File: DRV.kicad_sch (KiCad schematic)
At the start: 31 parts

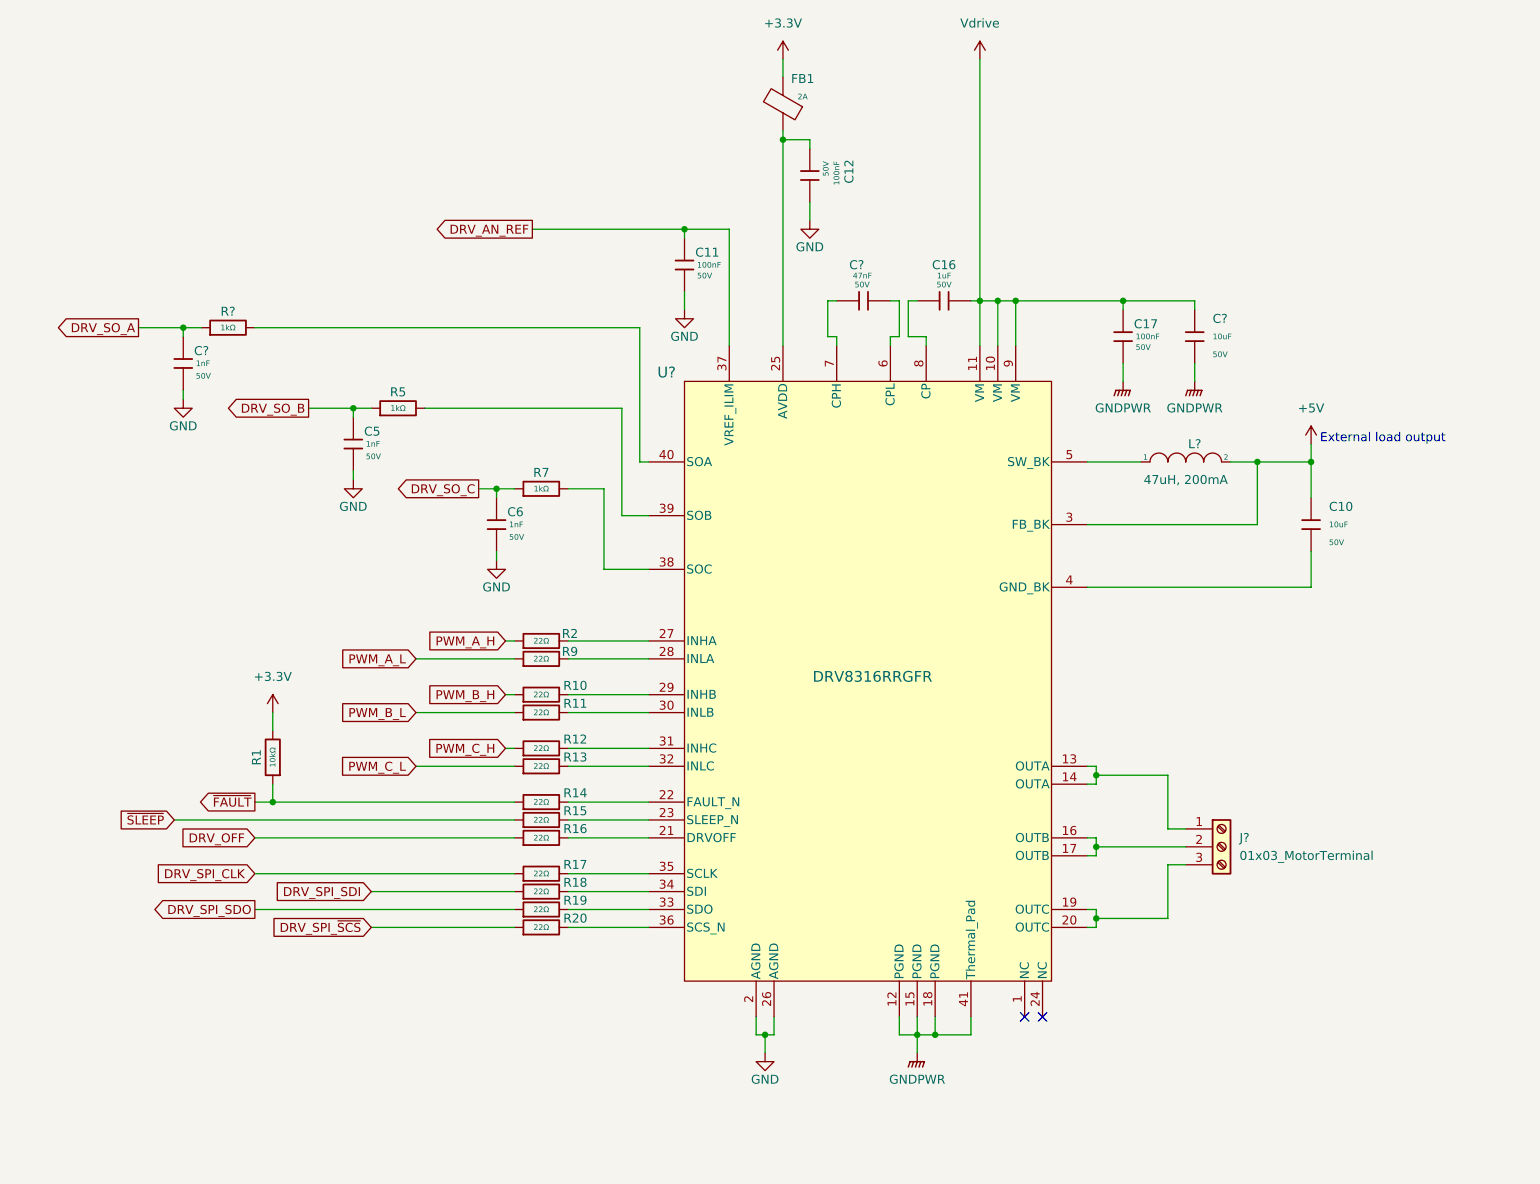
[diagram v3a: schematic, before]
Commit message: Add mcu connections
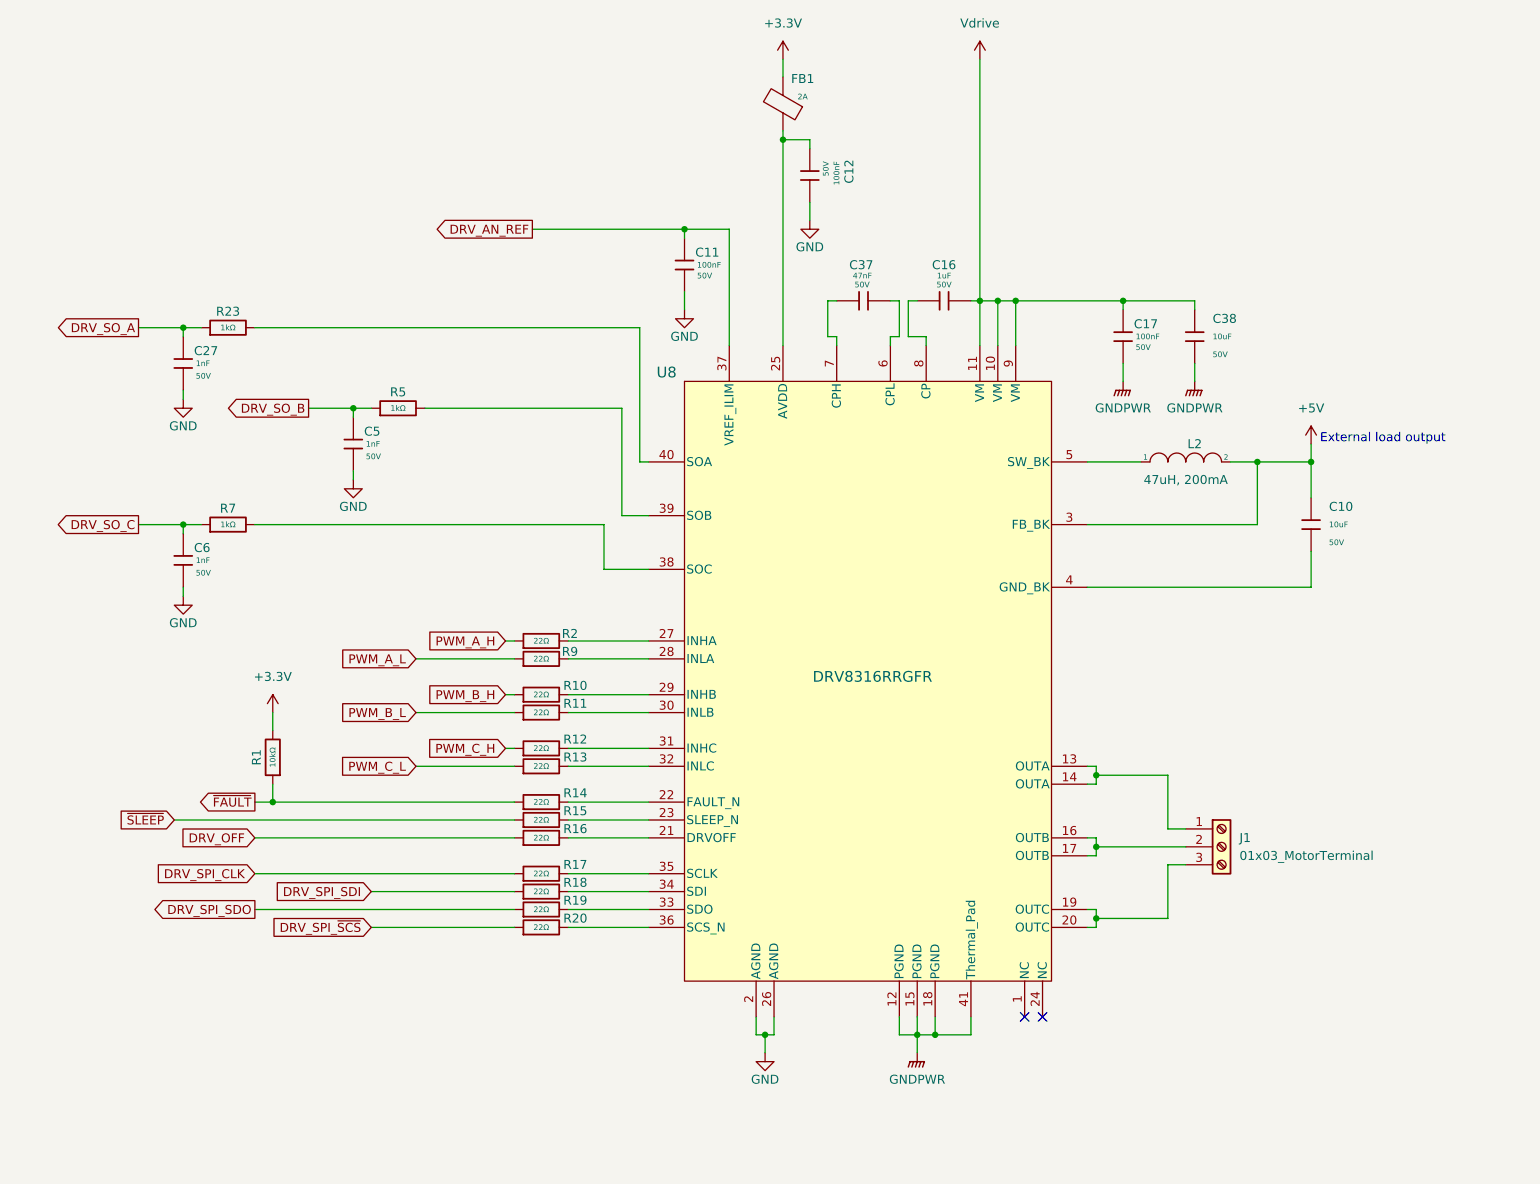
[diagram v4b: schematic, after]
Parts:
- U8: renamed from U?; footprint RGF0040E-IPC_A -> DRV8316:RGF0040E-IPC_A
- gave numbers to parts that had none: 6
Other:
- moved on the sheet: C6, R7

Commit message: Added DRV layout
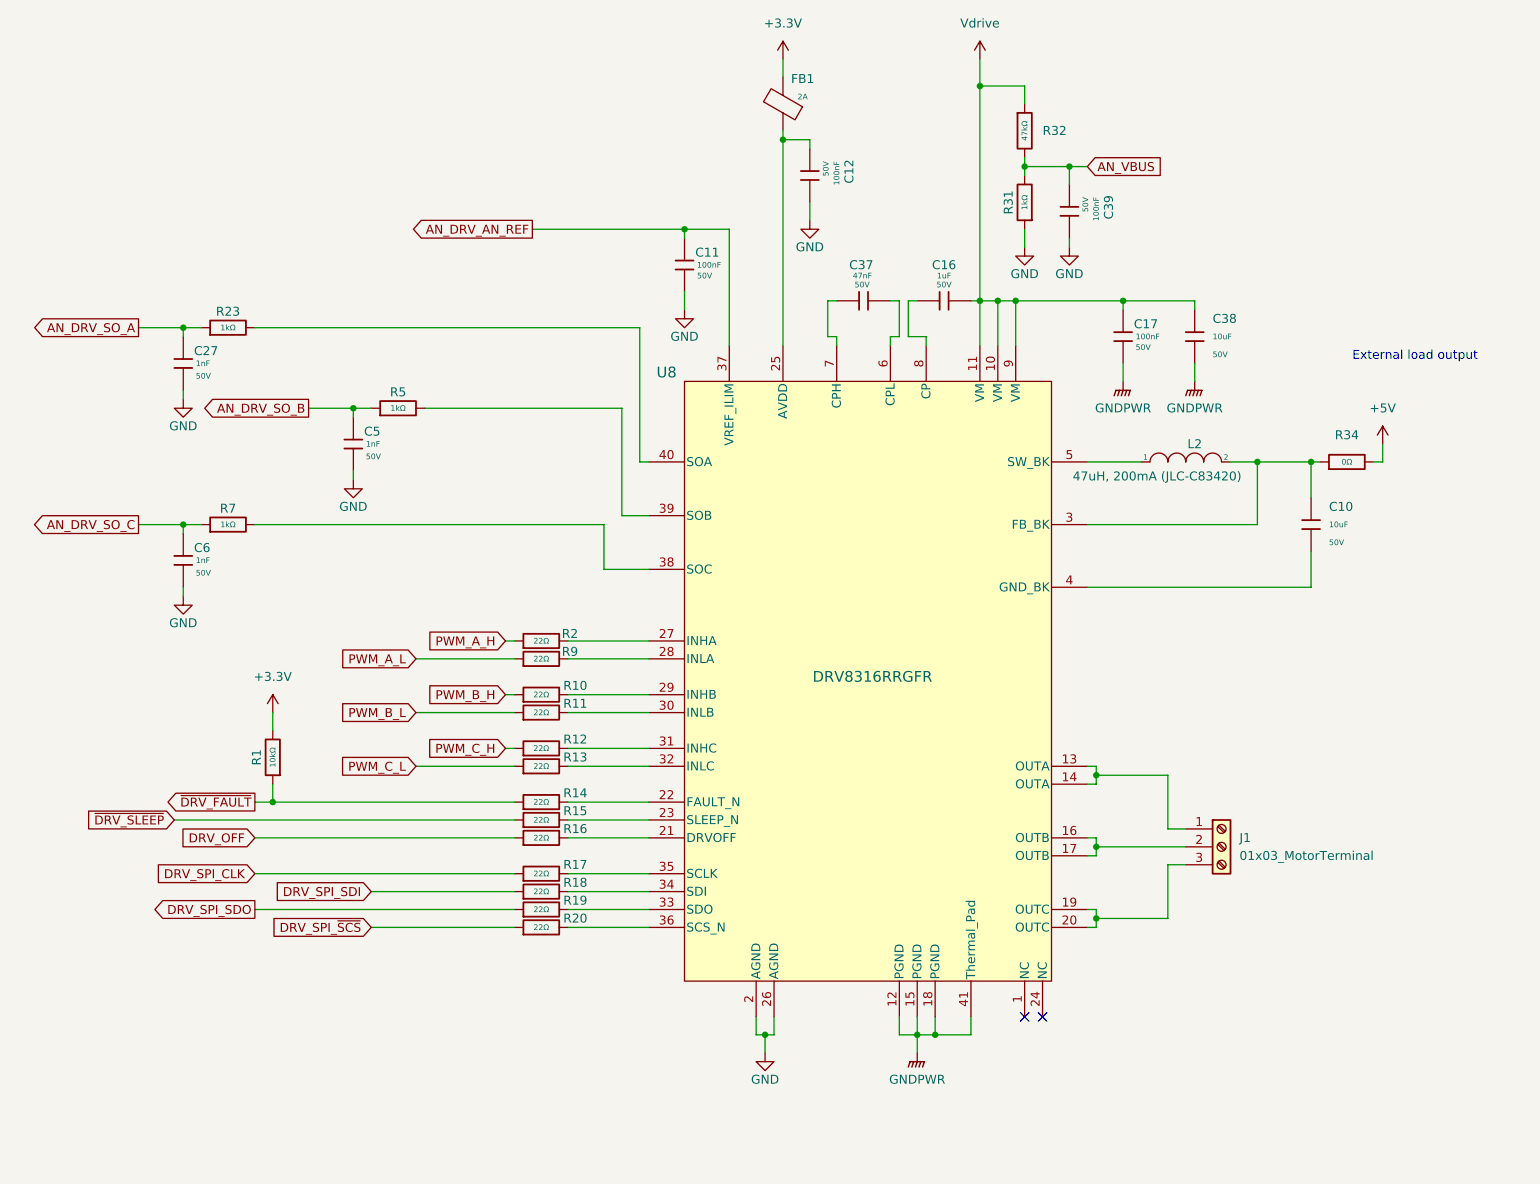
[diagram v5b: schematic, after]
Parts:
- added C39: 100nF, PCM_JLCPCB:C_0603, symbol PCM_JLCPCB-Capacitors:0603,100nF
- added R31: 1kΩ, PCM_JLCPCB:R_0603, symbol PCM_JLCPCB-Resistors:0603,1kΩ
- added R32: 47kΩ, PCM_JLCPCB:R_0603, symbol PCM_JLCPCB-Resistors:0603,47kΩ
- added R34: 0Ω, PCM_JLCPCB:R_0603, symbol PCM_JLCPCB-Resistors:0603,0Ω
- J1: footprint (none) -> Connector_Phoenix_MC:PhoenixContact_MC_1,5_3-G-3.5_1x03_P3.50mm_Horizontal
- L2: value 47uH, 200mA -> 47uH, 200mA (JLC-C83420); footprint (none) -> Inductor_SMD:L_Changjiang_FNR3010S
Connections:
- net +5V: now also R34.2; no longer C10.1, L2.2, U8.3 (FB_BK)
- net GND: now also C39.2, R31.1
- net Vdrive: now also R32.1
- net DRV_AN_REF renamed AN_DRV_AN_REF
- net DRV_SO_A renamed AN_DRV_SO_A
- net DRV_SO_B renamed AN_DRV_SO_B
- net DRV_SO_C renamed AN_DRV_SO_C
- net ~{FAULT} renamed ~{DRV_FAULT}
- net ~{SLEEP} renamed ~{DRV_SLEEP}
- new net: C10.1, L2.2, R34.1, U8.3 (FB_BK)
- new net AN_VBUS: C39.1, R31.2, R32.2

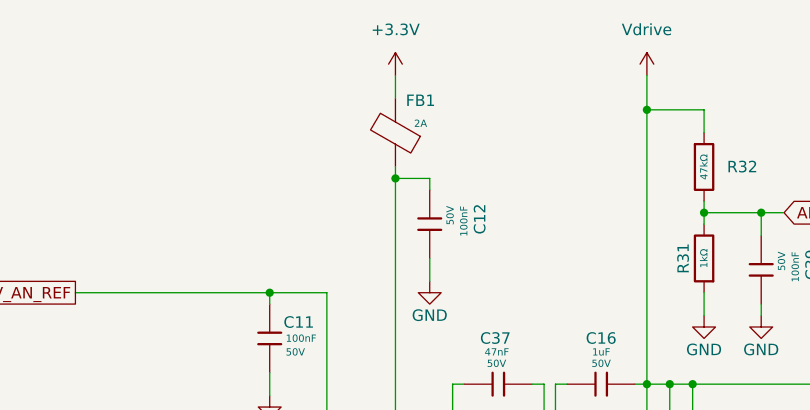
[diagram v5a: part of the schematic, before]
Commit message: updated mcu connections
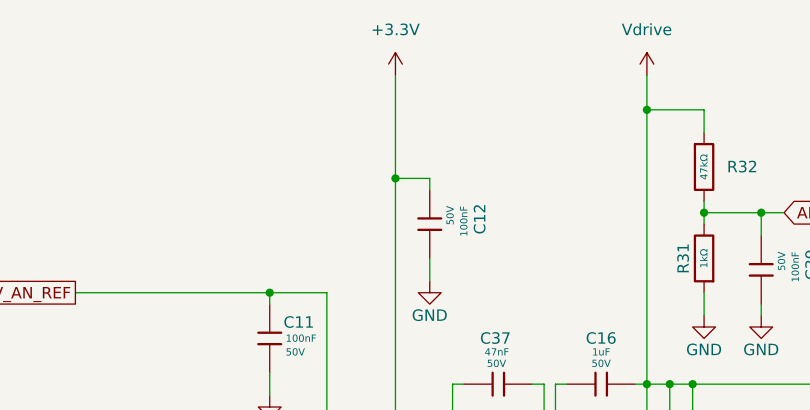
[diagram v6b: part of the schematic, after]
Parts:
- removed FB1: ~, PCM_JLCPCB:FB_0603, symbol PCM_JLCPCB-Inductors:Ferrite,0603,(2)
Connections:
- net +3.3V: now also C12.1, U8.25 (AVDD)
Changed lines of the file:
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@@
 	(wire
 		(pts
+			(xy 127 31.75) (xy 127 43.18)
+		)
+		(stroke
+			(width 0)
+			(type default)
+		)
+	)
+	(wire
+		(pts
 			(xy 171.45 154.94) (xy 170.18 154.94)
 		)
@@
 	(wire
 		(pts
-			(xy 127 41.91) (xy 127 43.18)
-		)
-		(stroke
-			(width 0)
-			(type default)
-		)
-	)
-	(wire
-		(pts
 			(xy 96.52 132.08) (xy 107.95 132.08)
 		)
@@
 	(wire
 		(pts
-			(xy 127 31.75) (xy 127 34.29)
-		)
-		(stroke
-			(width 0)
-			(type default)
-		)
-	)
-	(wire
-		(pts
 			(xy 171.45 132.08) (xy 171.45 133.35)
 		)
@@
 					(unit 1)
 				)
-			)
-		)
-	)
-	(symbol
-		(lib_id "PCM_JLCPCB-Inductors:Ferrite,0603,(2)")
-		(at 127 38.1 180)
-		(unit 1)
-		(exclude_from_sim no)
-		(in_bom yes)
-		(on_board yes)
-		(dnp no)
-		(property "Reference" "FB1"
-			(at 129.794 34.544 0)
-			(effects
-				(font
-					(size 1.27 1.27)
-				)
-			)
-		)
-		(property "Value" "~"
-			(at 129.794 35.814 0)
-			(effects
-				(font
-					(size 0.8 0.8)
-				)
-			)
-		)
-		(property "Footprint" "PCM_JLCPCB:FB_0603"
-			(at 128.778 38.1 90)
-			(effects
-				(font
-					(size 1.27 1.27)
-				)
-				(hide yes)
-			)
-		)
-		(property "Datasheet" "https://www.lcsc.com/datasheet/lcsc_datasheet_2304140030_Murata-Electronics-BLM18PG121SN1D_C14709.pdf"
-			(at 127 38.1 0)
-			(effects
-				(font
-					(size 1.27 1.27)
-				)
-				(hide yes)
-			)
-		)
-		(property "Description" "50mΩ ±25% 120Ω@100MHz 0603 Ferrite Beads ROHS"
-			(at 127 38.1 0)
-			(effects
-				(font
-					(size 1.27 1.27)
-				)
-				(hide yes)
-			)
-		)
-		(property "LCSC" "C14709"
-			(at 127 38.1 0)
-			(effects
-				(font
-					(size 1.27 1.27)
-				)
-				(hide yes)
-			)
-		)
-		(property "Stock" "222675"
-			(at 127 38.1 0)
-			(effects
-				(font
-					(size 1.27 1.27)
-				)
-				(hide yes)
-			)
-		)
-		(property "Price" "0.009USD"
-			(at 127 38.1 0)
-			(effects
-				(font
-					(size 1.27 1.27)
-				)
-				(hide yes)
-			)
-		)
-		(property "Process" "SMT"
-			(at 127 38.1 0)
-			(effects
-				(font
-					(size 1.27 1.27)
-				)
-				(hide yes)
-			)
-		)
-		(property "Minimum Qty" "20"
-			(at 127 38.1 0)
-			(effects
-				(font
-					(size 1.27 1.27)
-				)
-				(hide yes)
-			)
-		)
-		(property "Attrition Qty" "10"
-			(at 127 38.1 0)
-			(effects
-				(font
-					(size 1.27 1.27)
-				)
-				(hide yes)
-			)
-		)
-		(property "Class" "Basic Component"
-			(at 127 38.1 0)
-			(effects
-				(font
-					(size 1.27 1.27)
-				)
-				(hide yes)
-			)
-		)
-		(property "Category" "Filters/EMI Optimization,Ferrite Beads"
-			(at 127 38.1 0)
-			(effects
-				(font
-					(size 1.27 1.27)
-				)
-				(hide yes)
-			)
-		)
-		(property "Manufacturer" "Murata Electronics"
-			(at 127 38.1 0)
-			(effects
-				(font
-					(size 1.27 1.27)
-				)
-				(hide yes)
-			)
-		)
-		(property "Part" "BLM18PG121SN1D"
-			(at 127 38.1 0)
-			(effects
-				(font
-					(size 1.27 1.27)
-				)
-				(hide yes)
-			)
-		)
-		(property "DC Resistance" "50mΩ"
-			(at 127 38.1 0)
-			(effects
-				(font
-					(size 1.27 1.27)
-				)
-				(hide yes)
-			)
-		)
-		(property "Impedance @ Frequency" "120Ω@100MHz"
-			(at 127 38.1 0)
-			(effects
-				(font
-					(size 1.27 1.27)
-				)
-				(hide yes)
-			)
-		)
-		(property "Circuits" "1"
-			(at 127 38.1 0)
-			(effects
-				(font
-					(size 1.27 1.27)
-				)
-				(hide yes)
-			)
-		)
-		(property "Current Rating" "2A"
-			(at 129.794 37.084 0)
-			(effects
-				(font
-					(size 0.8 0.8)
-				)
-			)
-		)
-		(property "Tolerance" "±25%"
-			(at 127 38.1 0)
-			(effects
-				(font
-					(size 1.27 1.27)
-				)
-				(hide yes)
-			)
-		)
-		(pin "1"
-		)
-		(pin "2"
-		)
-		(instances
-			(project "PiccoloMotorDriver"
-				(path "/cc8a13e7-b1a6-4cbd-adcd-4feb8b2e2369/22171b38-2124-423e-bbc1-85af78cbc5a3"
-					(reference "FB1")
-					(unit 1)
-				)

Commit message: more layout
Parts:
- removed C10: 10uF, PCM_JLCPCB:C_1206, symbol PCM_JLCPCB-Capacitors:1206,10uF
- removed L2: 47uH, 200mA (JLC-C83420), Inductor_SMD:L_Changjiang_FNR3010S, symbol pspice:INDUCTOR
- removed R34: 0Ω, PCM_JLCPCB:R_0603, symbol PCM_JLCPCB-Resistors:0603,0Ω
- added TP7: GND_BK, TestPoint:TestPoint_Pad_D1.0mm, symbol Connector:TestPoint
- added TP8: FB_BK, TestPoint:TestPoint_Pad_D1.0mm, symbol Connector:TestPoint
- added TP9: SW_BK, TestPoint:TestPoint_Pad_D1.0mm, symbol Connector:TestPoint
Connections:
- net at U8.5 (SW_BK): now also TP9.1
- net at U8.3 (FB_BK): now also TP8.1
- net at U8.4 (GND_BK): now also TP7.1

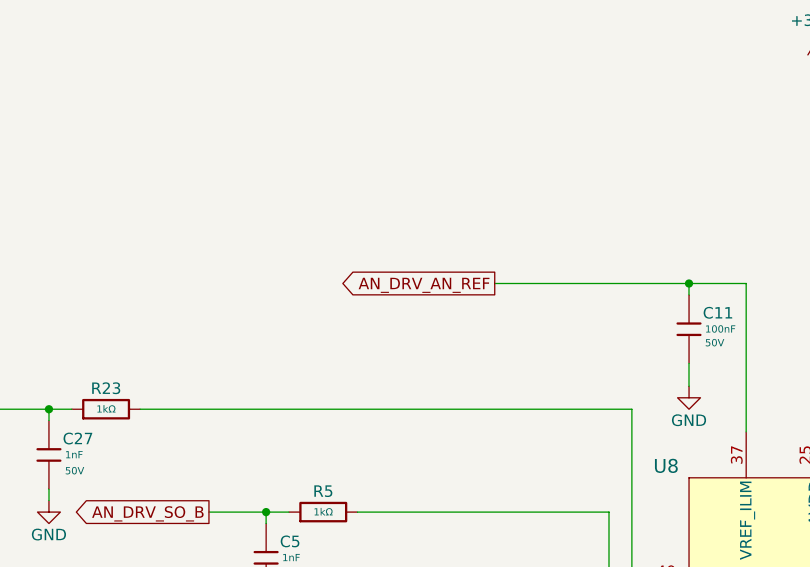
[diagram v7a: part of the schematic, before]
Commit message: Reroute mcu lines, updated can, motor timer pins
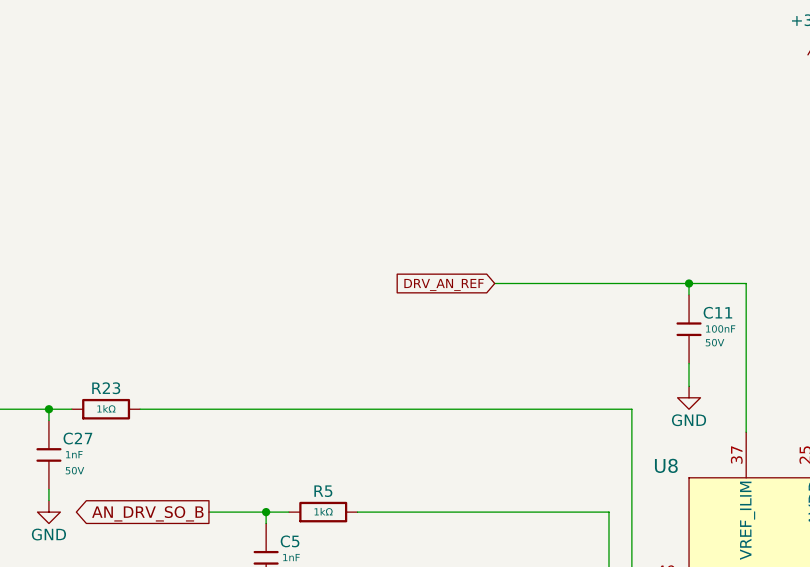
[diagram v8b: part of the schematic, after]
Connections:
- net AN_DRV_AN_REF renamed DRV_AN_REF
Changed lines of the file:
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@@
+		)
+	)
+	(global_label "DRV_AN_REF"
+		(shape input)
+		(at 91.44 55.88 180)
+		(fields_autoplaced yes)
+		(effects
+			(font
+				(size 1.016 1.016)
+				(color 0 144 255 1)
+			)
+			(justify right)
+		)
+		(property "Intersheetrefs" "${INTERSHEET_REFS}"
+			(at 79.8596 55.88 0)
+			(effects
+				(font
+					(size 1.27 1.27)
+				)
+				(justify right)
+				(hide yes)
+			)
 		)
 	)
@@
 			(effects
 				(font
-					(size 1.27 1.27)
-				)
-				(justify right)
-				(hide yes)
-			)
-		)
-	)
-	(global_label "AN_DRV_AN_REF"
-		(shape output)
-		(at 91.44 55.88 180)
-		(fields_autoplaced yes)
-		(effects
-			(font
-				(size 1.27 1.27)
-			)
-			(justify right)
-		)
-		(property "Intersheetrefs" "${INTERSHEET_REFS}"
-			(at 73.5776 55.88 0)
-			(effects
-				(font
